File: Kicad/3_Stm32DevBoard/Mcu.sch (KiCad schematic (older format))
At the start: 7 parts, among them J10 JST XH Buttons, J11 LCD JST XH, J12 Bypass Switch JST XH, J7 UART Pin Header, U3 ChinaBluePill

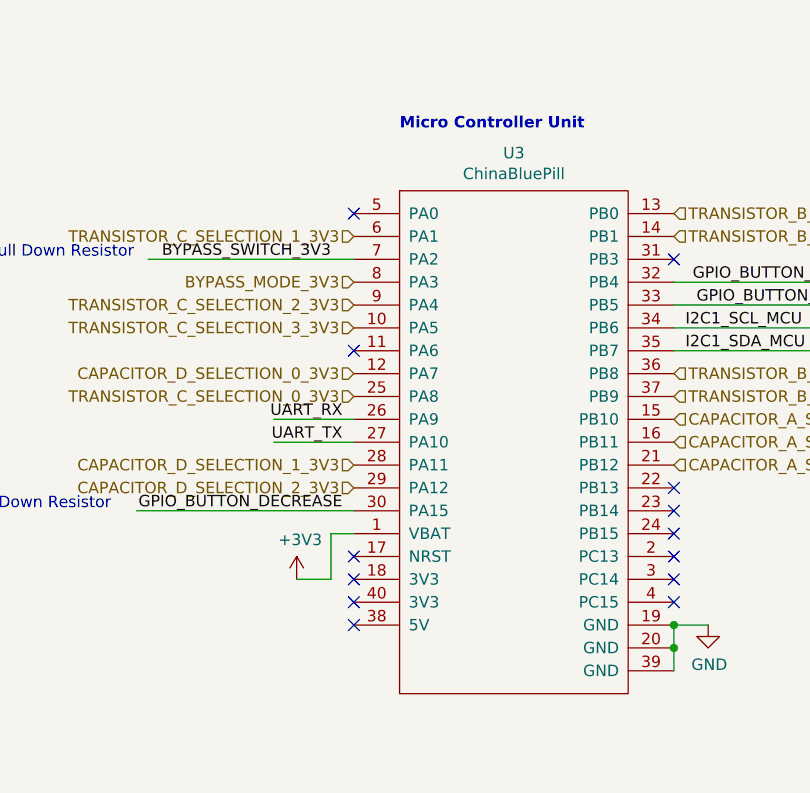
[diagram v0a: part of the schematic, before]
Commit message: Remove 3V3 voltage regulation (get from STM32 5V)
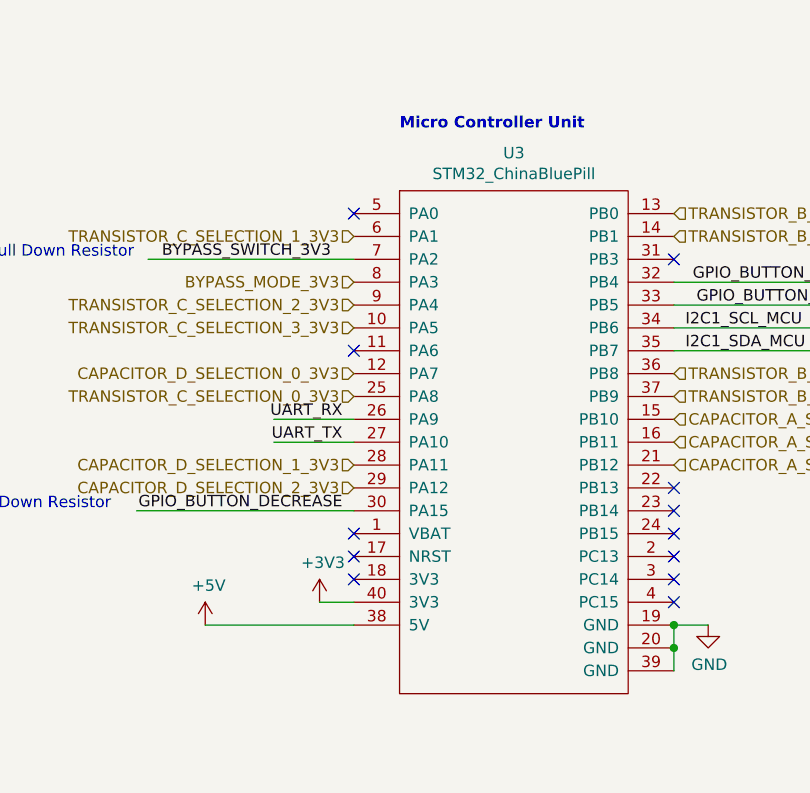
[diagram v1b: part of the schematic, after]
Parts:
- removed U3: ChinaBluePill, 3_Stm32DevBoard:BluePill_STM32F103C, symbol STM32a:ChinaBluePill
- added U3: STM32_ChinaBluePill, 3_Stm32DevBoard:BluePill_STM32F103C, symbol STM32a:STM32_ChinaBluePill
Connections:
- wire segments 40 -> 39
- no-connect marks 13 -> 12
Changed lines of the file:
@@
 	1    0    0    -1
 $EndComp
-$Comp
-L power:+3V3 #PWR046
-U 1 1 5E9950D9
-P 6900 3200
-F 0 "#PWR046" H 6900 3050 50  0001 C CNN
-F 1 "+3V3" H 6915 3373 50  0000 C CNN
-F 2 "" H 6900 3200 50  0001 C CNN
-F 3 "" H 6900 3200 50  0001 C CNN
-	1    6900 3200
-	1    0    0    -1
-$EndComp
-Wire Wire Line
-	6350 3200 6900 3200
 Text Label 7100 3300 2    50   ~ 0
 BYPASS_SWITCH_3V3
@@
 NoConn ~ 2300 2150
 NoConn ~ 2300 1550
-NoConn ~ 2300 3150
-NoConn ~ 2300 3250
 NoConn ~ 2300 3050
 $Comp
@@
 	1    0    0    -1
 $EndComp
-$Comp
-L power:+3V3 #PWR0109
-U 1 1 5ED7D950
-P 2050 3150
-F 0 "#PWR0109" H 2050 3000 50  0001 C CNN
-F 1 "+3V3" H 2065 3323 50  0000 C CNN
-F 2 "" H 2050 3150 50  0001 C CNN
-F 3 "" H 2050 3150 50  0001 C CNN
-	1    2050 3150
-	1    0    0    -1
-$EndComp
-Wire Wire Line
-	2050 3150 2200 3150
-Wire Wire Line
-	2200 3150 2200 2950
-Wire Wire Line
-	2200 2950 2300 2950
-$Comp
-L STM32a:ChinaBluePill U3
-U 1 1 5EDB9EF2
-P 3000 2100
-F 0 "U3" H 3000 2915 50  0000 C CNN
-F 1 "ChinaBluePill" H 3000 2824 50  0000 C CNN
-F 2 "3_Stm32DevBoard:BluePill_STM32F103C" H 3000 2100 50  0001 C CNN
-F 3 "" H 3000 2100 50  0001 C CNN
-	1    3000 2100
-	1    0    0    -1
-$EndComp
 Wire Wire Line
 	3700 3350 3850 3350
@@
 Wire Wire Line
 	3700 3450 3700 3550
-NoConn ~ 2300 3350
+NoConn ~ 2300 2950
 $Comp
 L Device:R R6
@@
 	0    1    1    0
 $EndComp
+Wire Wire Line
+	2300 3350 1650 3350
+$Comp
+L power:+5V #PWR0104
+U 1 1 5F008F98
+P 1650 3350
+F 0 "#PWR0104" H 1650 3200 50  0001 C CNN
+F 1 "+5V" H 1665 3523 50  0000 C CNN
+F 2 "" H 1650 3350 50  0001 C CNN
+F 3 "" H 1650 3350 50  0001 C CNN
+	1    1650 3350
+	1    0    0    -1
+$EndComp
+$Comp
+L power:+3V3 #PWR046
+U 1 1 5E9950D9
+P 6900 3200
+F 0 "#PWR046" H 6900 3050 50  0001 C CNN
+F 1 "+3V3" H 6915 3373 50  0000 C CNN
+F 2 "" H 6900 3200 50  0001 C CNN
+F 3 "" H 6900 3200 50  0001 C CNN
+	1    6900 3200
+	1    0    0    -1
+$EndComp
+Wire Wire Line
+	6350 3200 6900 3200
+$Comp
+L power:+3V3 #PWR0109
+U 1 1 5F019E0C
+P 2150 3250
+F 0 "#PWR0109" H 2150 3100 50  0001 C CNN
+F 1 "+3V3" H 2165 3423 50  0000 C CNN
+F 2 "" H 2150 3250 50  0001 C CNN
+F 3 "" H 2150 3250 50  0001 C CNN
+	1    2150 3250
+	1    0    0    -1
+$EndComp
+Wire Wire Line
+	2300 3250 2150 3250
+NoConn ~ 2300 3150
+$Comp
+L STM32a:STM32_ChinaBluePill U3
+U 1 1 5F02CD91
+P 3000 2100
+F 0 "U3" H 3000 2915 50  0000 C CNN
+F 1 "STM32_ChinaBluePill" H 3000 2824 50  0000 C CNN
+F 2 "3_Stm32DevBoard:BluePill_STM32F103C" H 3000 2100 50  0001 C CNN
+F 3 "" H 3000 2100 50  0001 C CNN
+	1    3000 2100
+	1    0    0    -1
+$EndComp
 $EndSCHEMATC
